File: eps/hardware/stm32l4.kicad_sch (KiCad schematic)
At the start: 32 parts, among them J13 Conn_ARM_JTAG_SWD_10, SW1 SW_Push, SW2 SW_SPDT, U10 STM32L496ZGTx, Y1 8MHz, Y2 32KHz

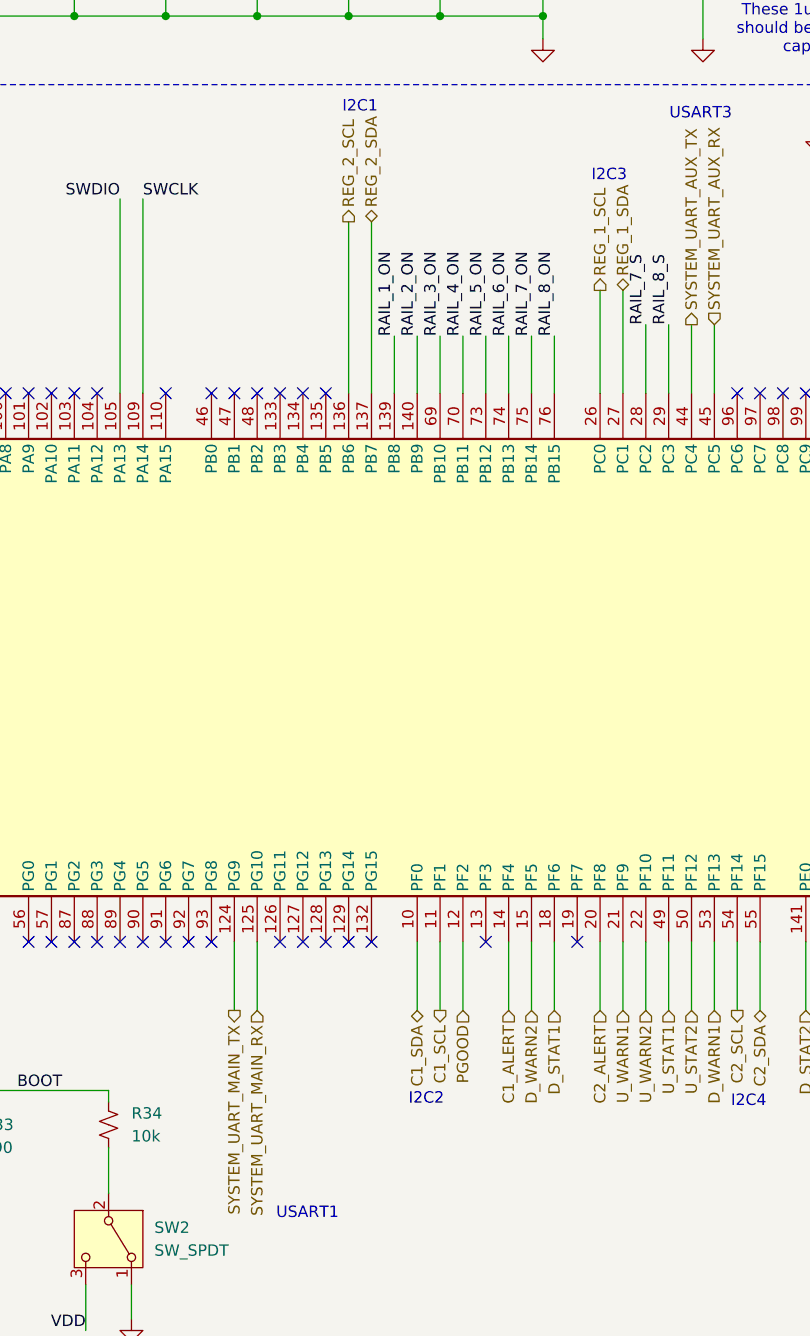
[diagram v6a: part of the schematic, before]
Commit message: start routing i2c signals
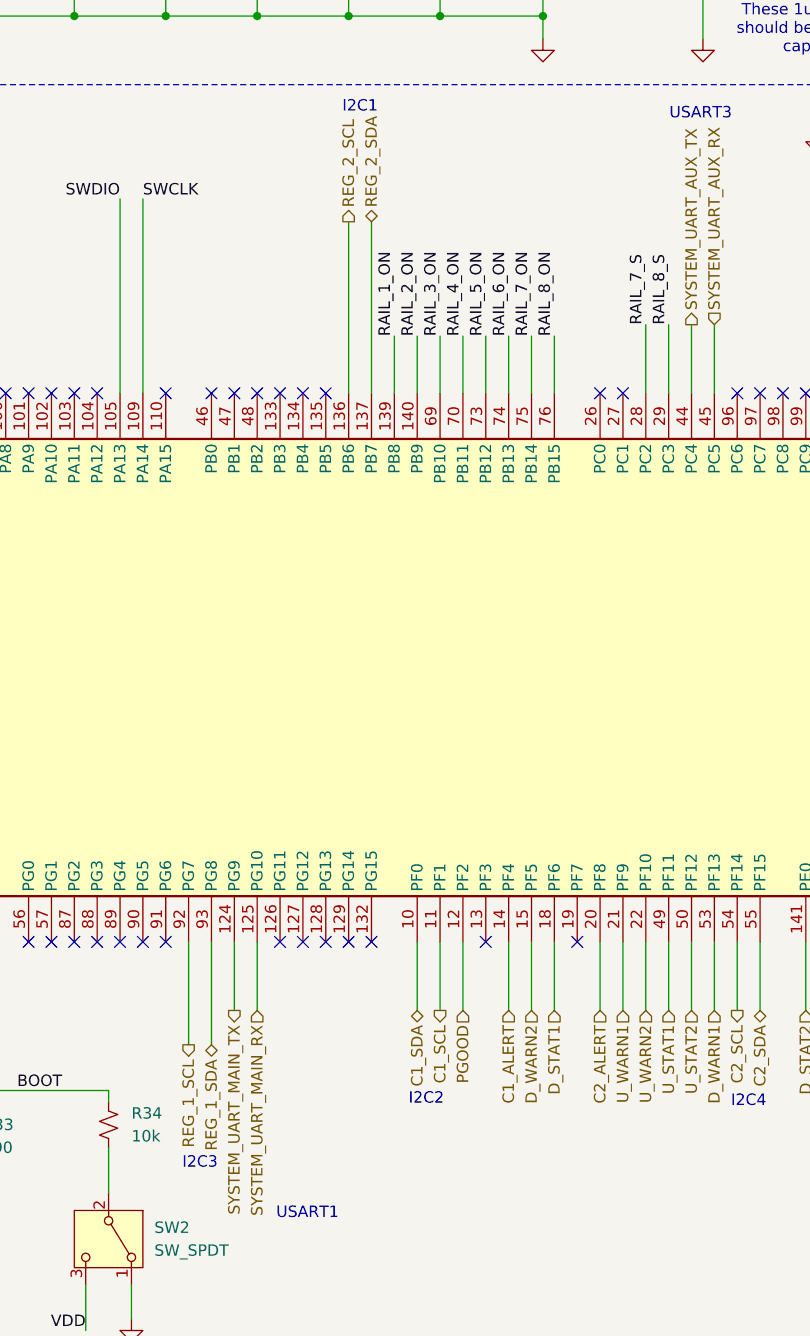
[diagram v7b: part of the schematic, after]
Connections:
- net REG_1_SCL: now also U10.92 (PG7); no longer U10.26 (PC0)
- net REG_1_SDA: now also U10.93 (PG8); no longer U10.27 (PC1)
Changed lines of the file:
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@@
 		)
 	)
-	(text "I2C3"
-		(exclude_from_sim no)
-		(at 154.686 52.07 0)
-		(effects
-			(font
-				(size 1.27 1.27)
-			)
-		)
-	)
 	(text "These 1uF bulk caps\nshould be a Tantalum\ncapacitor."
 		(exclude_from_sim no)
@@
 		)
 	)
+	(text "I2C3"
+		(exclude_from_sim no)
+		(at 109.22 161.798 0)
+		(effects
+			(font
+				(size 1.27 1.27)
+			)
+		)
+	)
 	(text "USART1"
 		(exclude_from_sim no)
@@
 	)
 	(no_connect
-		(at 110.49 137.16)
-	)
-	(no_connect
 		(at 95.25 76.2)
 	)
@@
 	)
 	(no_connect
+		(at 156.21 76.2)
+	)
+	(no_connect
 		(at 204.47 137.16)
 	)
@@
 	)
 	(no_connect
-		(at 107.95 137.16)
-	)
-	(no_connect
 		(at 173.99 76.2)
 	)
@@
 		(at 115.57 76.2)
 	)
+	(no_connect
+		(at 153.67 76.2)
+	)
 	(wire
 		(pts
@@
 	(wire
 		(pts
+			(xy 110.49 137.16) (xy 110.49 148.59)
+		)
+		(stroke
+			(width 0)
+			(type default)
+		)
+	)
+	(wire
+		(pts
 			(xy 184.15 137.16) (xy 184.15 144.78)
 		)
@@
 	(wire
 		(pts
-			(xy 156.21 64.77) (xy 156.21 76.2)
-		)
-		(stroke
-			(width 0)
-			(type default)
-		)
-	)
-	(wire
-		(pts
 			(xy 54.61 104.14) (xy 54.61 106.68)
 		)
@@
 	(wire
 		(pts
-			(xy 153.67 64.77) (xy 153.67 76.2)
-		)
-		(stroke
-			(width 0)
-			(type default)
-		)
-	)
-	(wire
-		(pts
 			(xy 189.23 137.16) (xy 189.23 144.78)
 		)
@@
 	(wire
 		(pts
+			(xy 107.95 137.16) (xy 107.95 148.59)
+		)
+		(stroke
+			(width 0)
+			(type default)
+		)
+	)
+	(wire
+		(pts
 			(xy 125.73 24.13) (xy 135.89 24.13)
 		)
@@
 		)
 	)
+	(hierarchical_label "REG_1_SCL"
+		(shape output)
+		(at 107.95 148.59 270)
+		(effects
+			(font
+				(size 1.27 1.27)
+			)
+			(justify right)
+		)
+	)
 	(hierarchical_label "REG_2_SDA"
 		(shape bidirectional)
@@
 		)
 	)
+	(hierarchical_label "REG_1_SDA"
+		(shape bidirectional)
+		(at 110.49 148.59 270)
+		(effects
+			(font
+				(size 1.27 1.27)
+			)
+			(justify right)
+		)
+	)
 	(hierarchical_label "D_WARN1"
 		(shape input)
@@
 		)
 	)
-	(hierarchical_label "REG_1_SCL"
-		(shape output)
-		(at 153.67 64.77 90)
-		(effects
-			(font
-				(size 1.27 1.27)
-			)
-			(justify left)
-		)
-	)
 	(hierarchical_label "RAIL_7_ADC"
 		(shape input)
@@
 		)
 	)
-	(hierarchical_label "REG_1_SDA"
-		(shape bidirectional)
-		(at 156.21 64.77 90)
-		(effects
-			(font
-				(size 1.27 1.27)
-			)
-			(justify left)
-		)
-	)

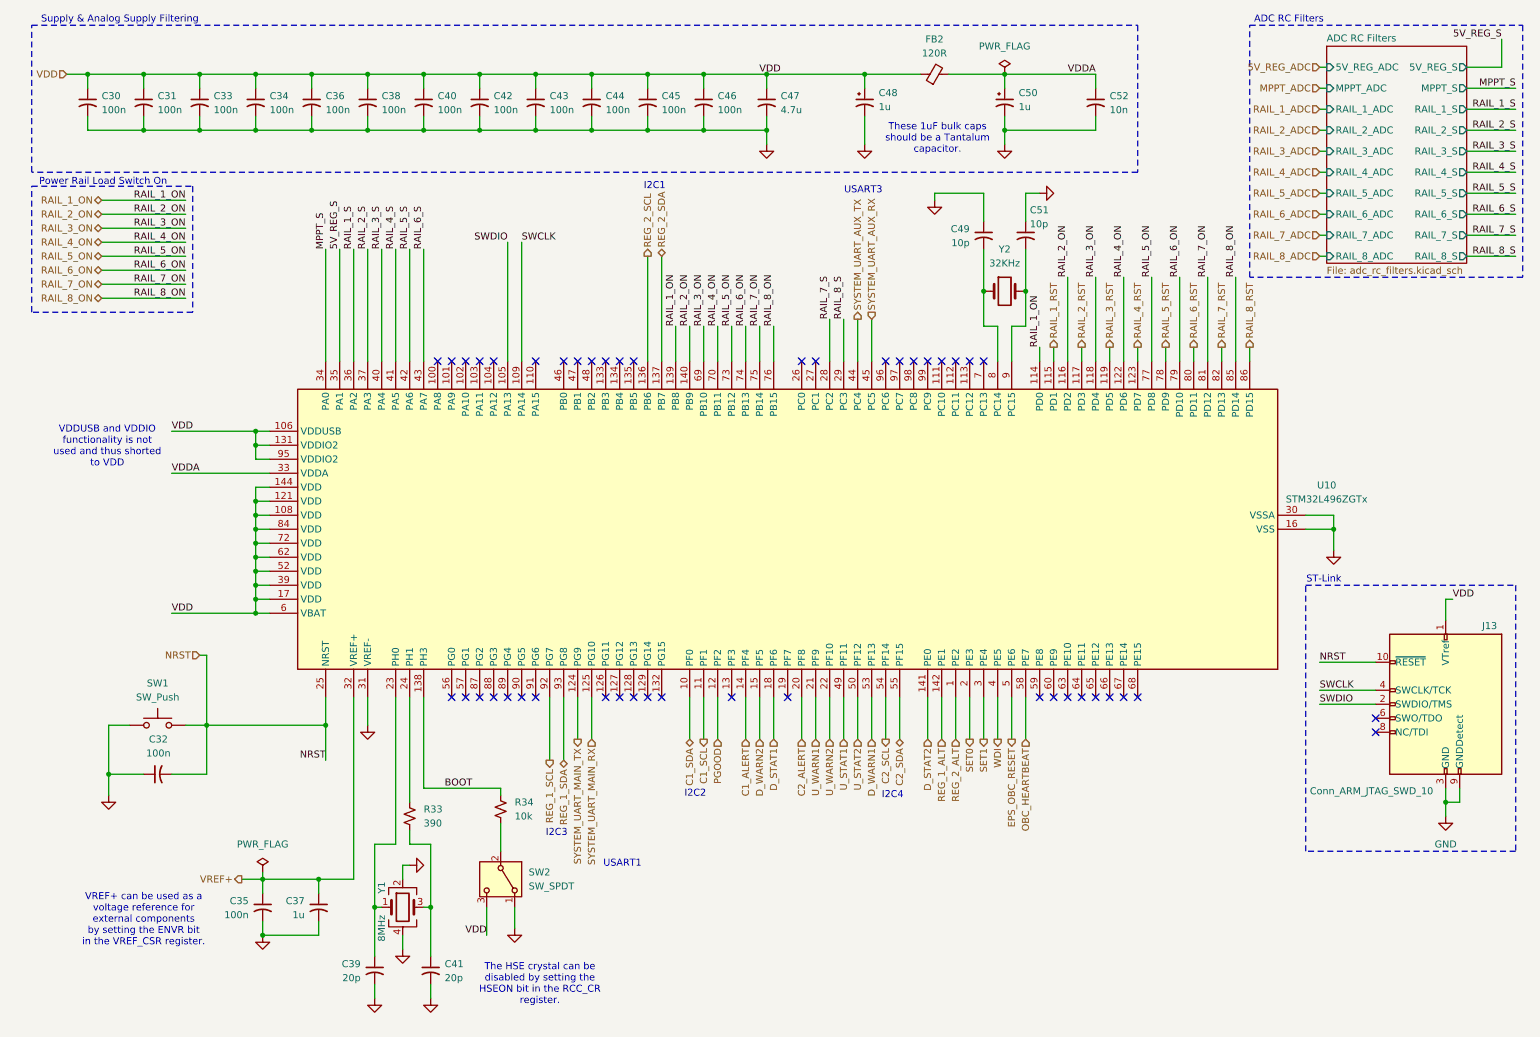
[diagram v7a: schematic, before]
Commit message: add BOM and fix tons of hardware bugs
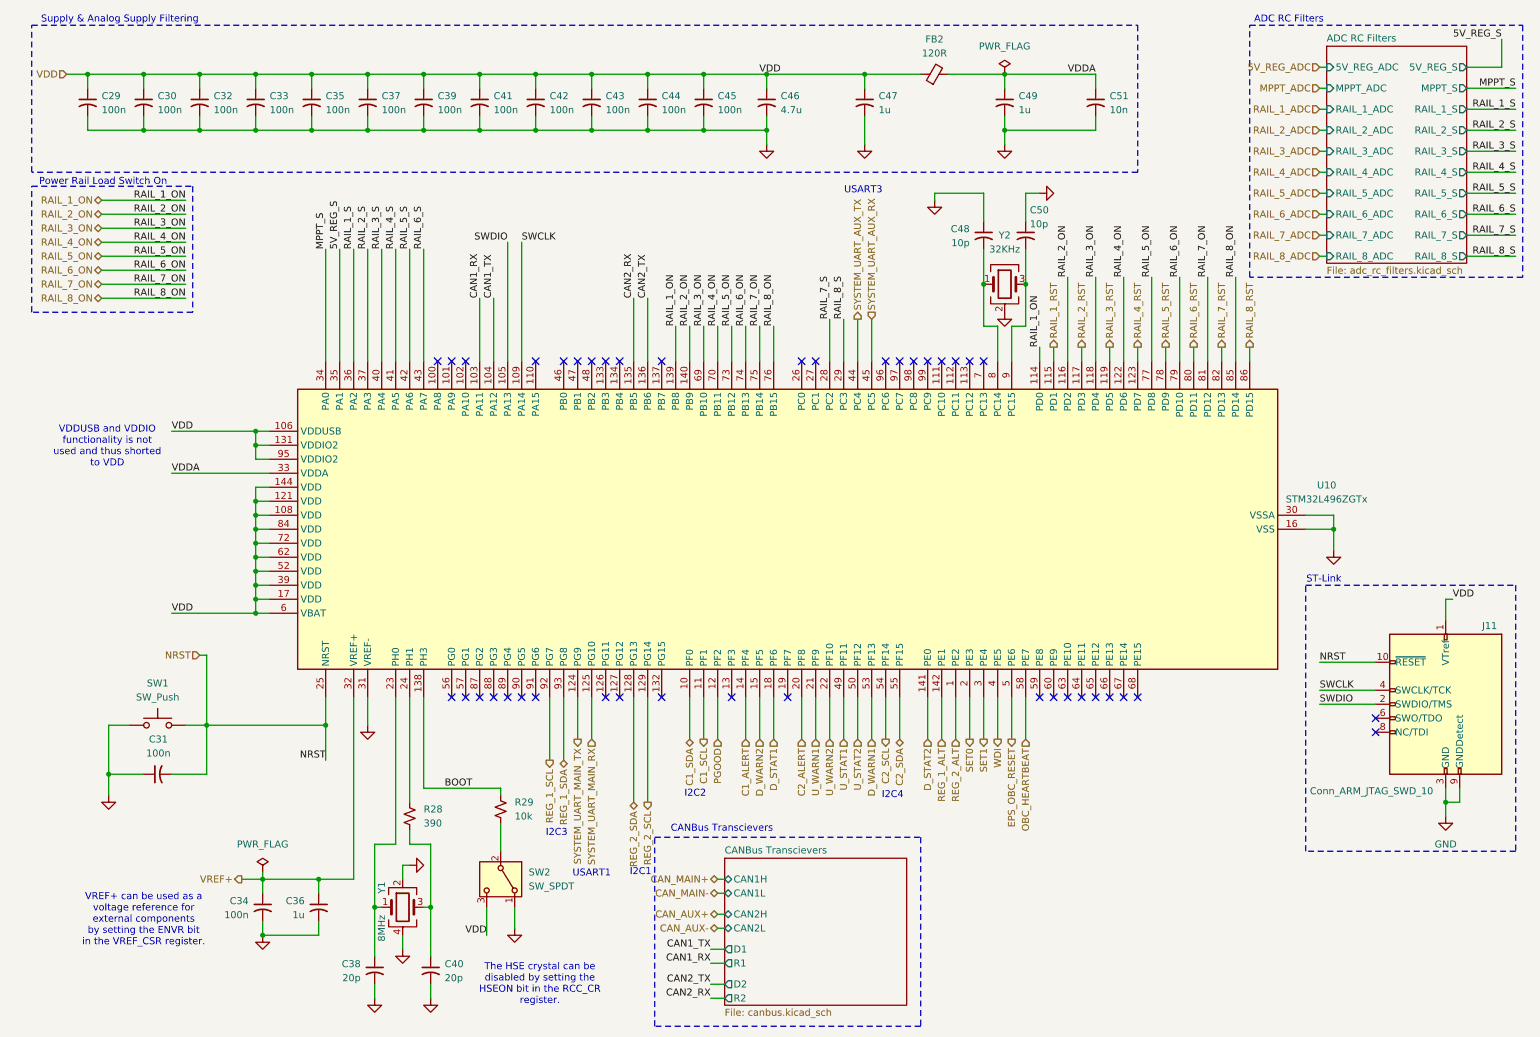
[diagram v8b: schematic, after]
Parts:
- removed C48, C50: 1u, Capacitor_Tantalum_SMD:CP_EIA-3216-18_Kemet-A, symbol Device:C_Polarized_Small_US
- added C47, C49: 1u, Capacitor_SMD:C_0805_2012Metric, symbol Device:C_Small_US
- C29: renamed from C30; LCSC PN (none) -> C1525
- C30: renamed from C31; LCSC PN (none) -> C1525
- C31: renamed from C32; LCSC PN (none) -> C1525
- C32: renamed from C33; LCSC PN (none) -> C1525
- C33: renamed from C34; LCSC PN (none) -> C1525
- C34: renamed from C35; LCSC PN (none) -> C1525
- C35: renamed from C36; LCSC PN (none) -> C1525
- C36: renamed from C37; LCSC PN (none) -> C29266
- C37: renamed from C38; LCSC PN (none) -> C1525
- C38: renamed from C39; LCSC PN (none) -> C1513151
- C39: renamed from C40; LCSC PN (none) -> C1525
- C40: renamed from C41; LCSC PN (none) -> C1513151
- C41: renamed from C42; LCSC PN (none) -> C1525
- C42: renamed from C43; LCSC PN (none) -> C1525
- C43: renamed from C44; LCSC PN (none) -> C1525
- C44: renamed from C45; LCSC PN (none) -> C1525
- C45: renamed from C46; LCSC PN (none) -> C1525
- C46: renamed from C47; LCSC PN (none) -> C29266
- C48: renamed from C49; LCSC PN (none) -> C2191950
- C50: renamed from C51; LCSC PN (none) -> C2191950
- C51: renamed from C52; LCSC PN (none) -> C85735
- FB2: LCSC PN (none) -> C338244
- R28: renamed from R33; LCSC PN (none) -> C25109
- SW1: LCSC PN (none) -> C115357
- SW2: LCSC PN (none) -> C221841
- U10: LCSC PN (none) -> C1337220
- Y1: LCSC PN C9002 -> C454610
- Y2: footprint Crystal:Crystal_SMD_3215-2Pin_3.2x1.5mm -> Crystal:Crystal_SMD_3225-4Pin_3.2x2.5mm; symbol Device:Crystal -> Device:Crystal_GND24; LCSC PN (none) -> C252344
- renumbered J13 to J11, R34 to R29
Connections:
- net GND: now also Y2.2 (G), Y2.4 (G), C47.2, C49.2
- net REG_2_SCL: now also U10.129 (PG14); no longer U10.136 (PB6)
- net REG_2_SDA: now also U10.128 (PG13); no longer U10.137 (PB7)
- net VDD: now also C47.1
- net VDDA: now also C49.1
- net CAN1_RX: now reaches U10.103 (PA11)
- net CAN1_TX: now reaches U10.104 (PA12)
- net CAN2_RX: now reaches U10.135 (PB5)
- net at C50.2, U10.9 (PC15): now also Y2.3; no longer Y2.2
- new net CAN2_TX: U10.136 (PB6)
- no-connect marks 46 -> 42
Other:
- added sheet CANBus Transcievers (canbus.kicad_sch)
- note added: "CANBus Transcievers"
- note removed: "These 1uF bulk caps should be a Tantalum capacitor."
